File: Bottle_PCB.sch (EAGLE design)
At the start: 78 parts, among them J1 GROVE-4P-2.0-SMD, Q1 8.000 MHz, Q2 ZVN 3306 F, Q3 ZVN 3306 F, Q4 ZVN 3306 F, Q5 ZVN 3306 F, Q6 ZVN 3306 F, Q7 ZVN 3306 F, U1 USD-SOCKETNEW

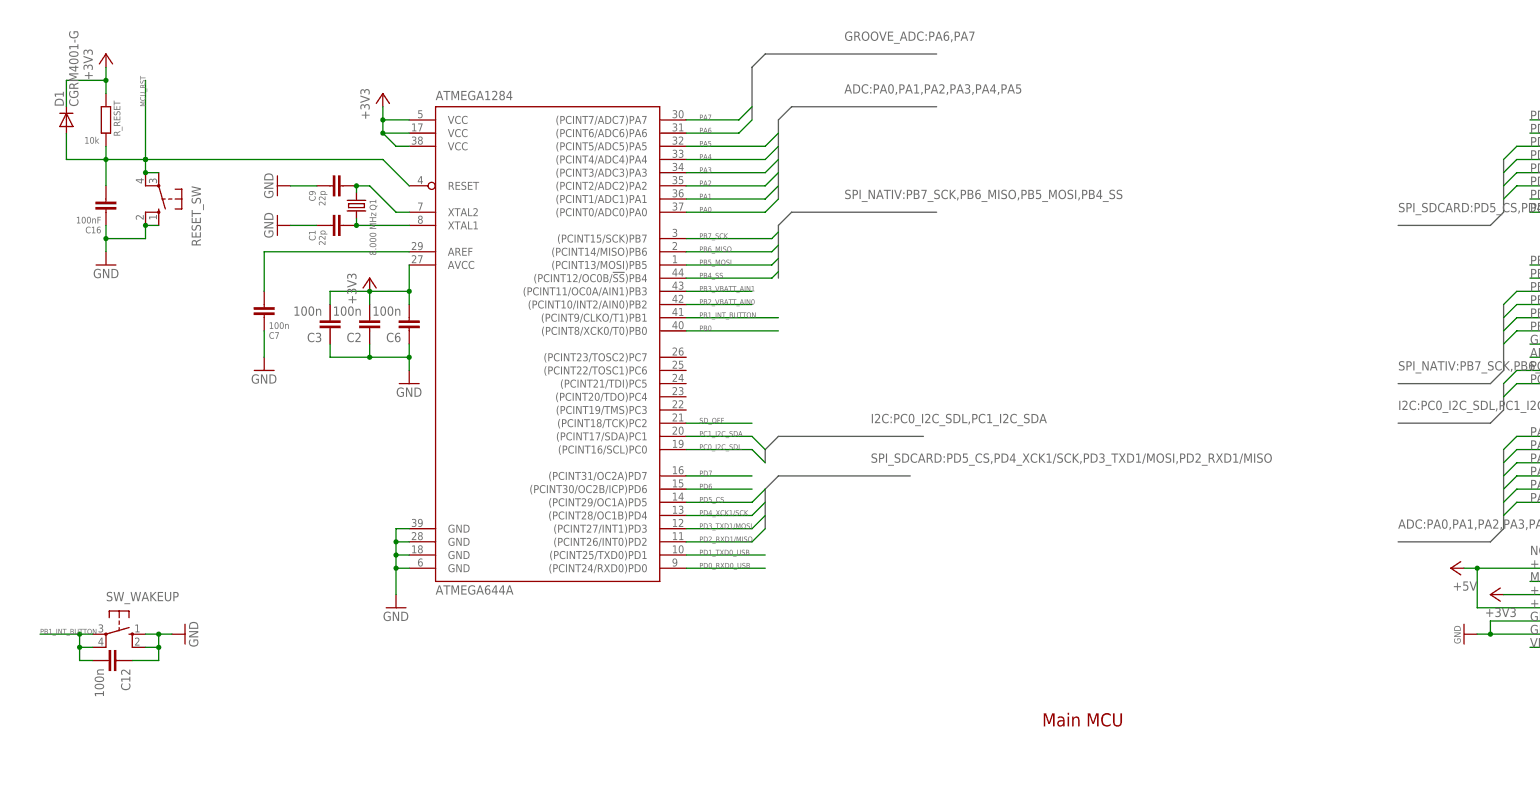
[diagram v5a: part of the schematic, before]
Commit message: - added some more frames for structure
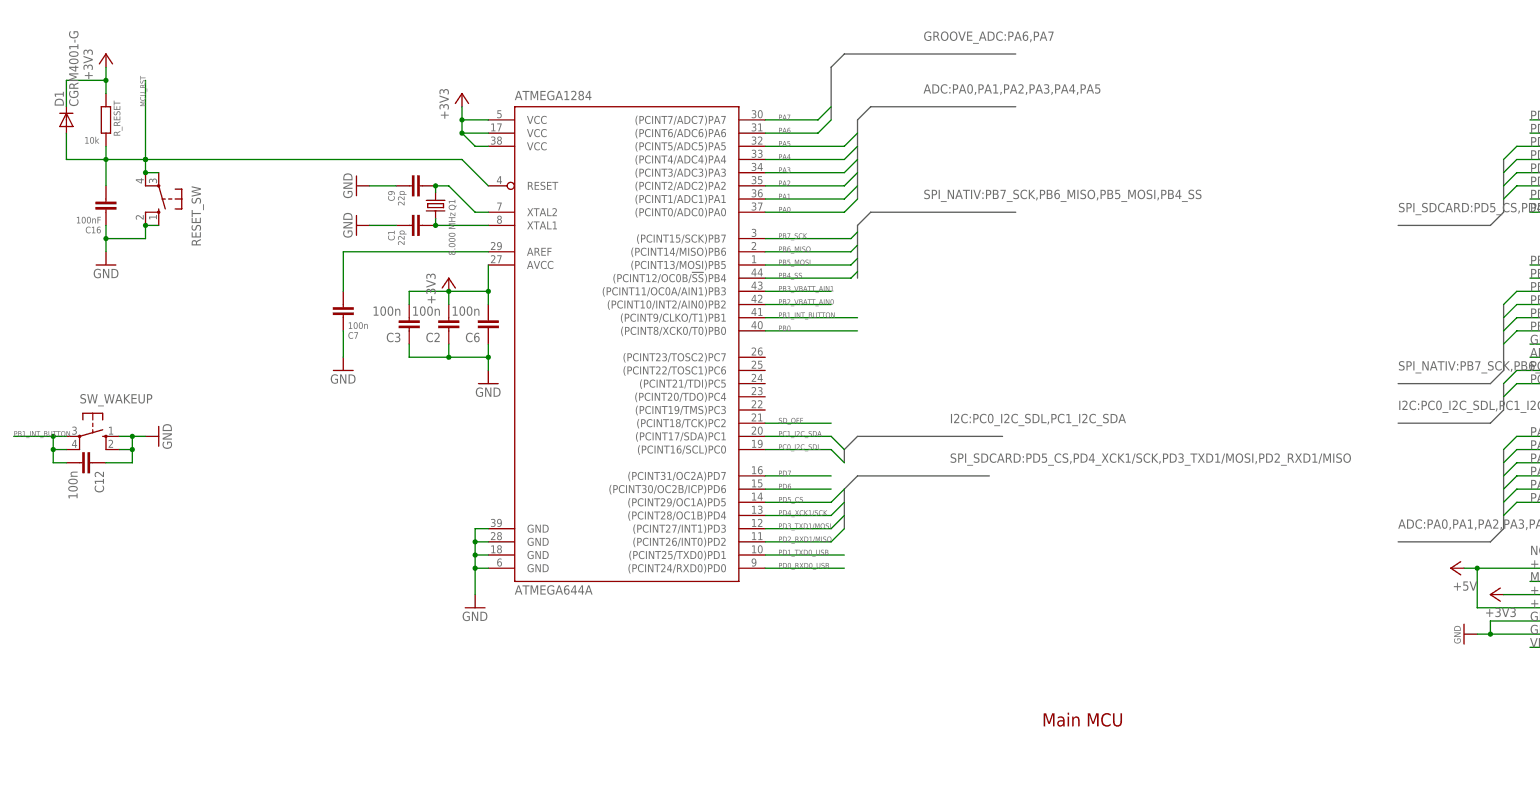
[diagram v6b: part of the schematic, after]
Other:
- note added: "MCU Reset"
- note added: "Main Microcontroller Unit"
- moved on the sheet: ATMEGA1284, C1, C12, C2, C3, C6, C7, C9, Q1, SW_WAKEUP

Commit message: - overhauled and simplified SD card connection - decided to stick with the sparkfun socket, as it's cheap and available by now
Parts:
- removed Q2, Q3, Q4: ZVN 3306 F, transistor-small-signal:BSS123
- removed R1: 50k, rcl:R-EU_M1206
- removed SJ1, SJ2: (no value), jumper:SJ2W
- R2: value 50k -> 10k
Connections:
- net SD_OFF renamed PC2_SD_OFF
- removed net N$16: SJ2.2, U1.SHIELD@2
- removed net N$17: SJ1.2, U1.SHIELD@4
- removed net N$21: R1.2, SJ2.3
- removed net N$22: R2.2, SJ1.1
- removed net N$28: Q4.D, U1.CS
- removed net N$29: Q3.D, U1.DI
- removed net N$30: Q2.D, U1.SCK
- new net PC3_SD_CD: ATMEGA1284.(PCINT19/TMS)PC3, R2.2, U1.SHIELD@2, U1.SHIELD@4
- net +3V3: no longer R1.1
- net GND: no longer SJ1.3, SJ2.1
- net N$33: no longer Q2.G, Q3.G, Q4.G
- net PD3_TXD1/MOSI: now also U1.DI; no longer Q3.S
- net PD4_XCK1/SCK: now also U1.SCK; no longer Q2.S
- net PD5_CS: now also U1.CS; no longer Q4.S
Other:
- note added: "CD pins are connected to GND when no card is insertet, and float if card is inserted. Thus, a pullup is needed for detection."
- moved on the sheet: C4, C5, Q5, R2, R5, R6, U1

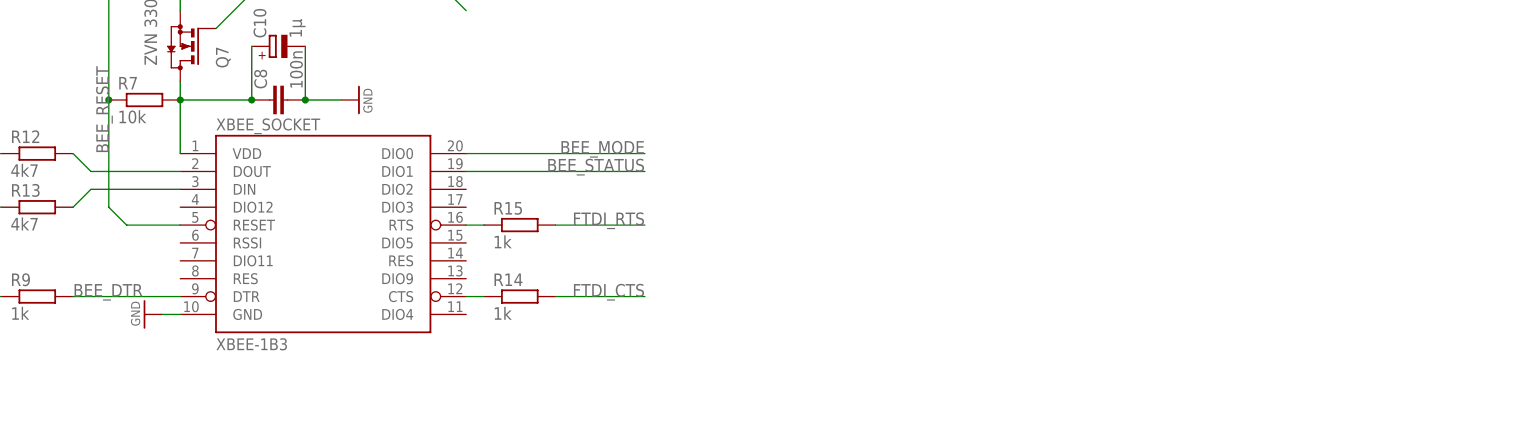
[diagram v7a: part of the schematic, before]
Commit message: - added HM11 BT Module - employed component device exported from SeedStudio BLE_Bee_v1.0 schematic
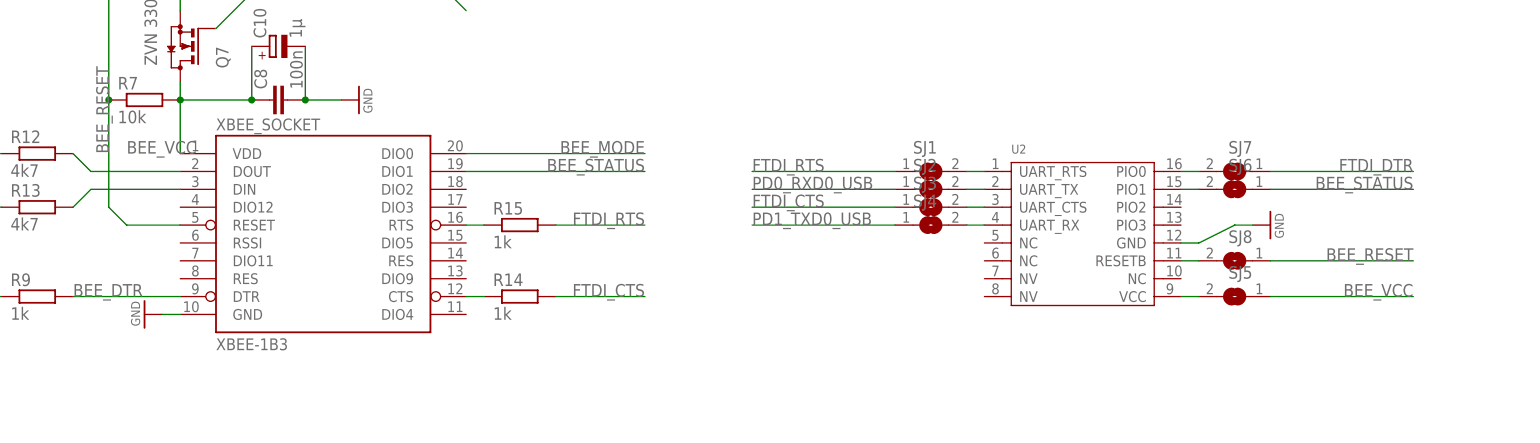
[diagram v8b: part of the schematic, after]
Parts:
- added SJ1, SJ2, SJ3, SJ4, SJ5, SJ6, SJ7, SJ8: (no value), jumper:SJ
- added U2: (no value), Seed-HM11:HM-11
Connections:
- new net N$16: SJ1.2, U2.UART_RTS
- new net N$17: SJ2.2, U2.UART_TX
- new net N$19: SJ3.2, U2.UART_CTS
- new net N$20: SJ4.2, U2.UART_RX
- new net N$21: SJ5.2, U2.VCC
- new net N$24: SJ8.2, U2.RESETB
- new net N$25: SJ6.2, U2.PIO1
- new net N$26: SJ7.2, U2.PIO0
- net BEE_RESET: now also SJ8.1
- net BEE_STATUS: now also SJ6.1
- net BEE_VCC: now also SJ5.1
- net FTDI_CTS: now also SJ3.1
- net FTDI_DTR: now also SJ7.1
- net FTDI_RTS: now also SJ1.1
- net GND: now also U2.GND
- net PD0_RXD0_USB: now also SJ2.1
- net PD1_TXD0_USB: now also SJ4.1
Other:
- note added: "HM11 BT Module"
- note removed: "BTBee Pro"
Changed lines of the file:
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@@
 <layer number="56" name="wert" color="7" fill="1" visible="no" active="no"/>
 <layer number="57" name="tCAD" color="7" fill="1" visible="no" active="no"/>
+<layer number="90" name="Modules" color="5" fill="1" visible="yes" active="yes"/>
 <layer number="91" name="Nets" color="2" fill="1" visible="yes" active="yes"/>
 <layer number="92" name="Busses" color="1" fill="1" visible="yes" active="yes"/>
@@
 <part name="R14" library="resistor" deviceset="R-EU_" device="R0603" value="1k"/>
 <part name="R15" library="resistor" deviceset="R-EU_" device="R0603" value="1k"/>
+<part name="U2" library="Seed-HM11" deviceset="HM-11" device=""/>
+<part name="SJ1" library="jumper" deviceset="SJ" device=""/>
+<part name="SJ2" library="jumper" deviceset="SJ" device=""/>
+<part name="SJ3" library="jumper" deviceset="SJ" device=""/>
+<part name="SJ4" library="jumper" deviceset="SJ" device=""/>
+<part name="SJ5" library="jumper" deviceset="SJ" device=""/>
+<part name="SJ6" library="jumper" deviceset="SJ" device=""/>
+<part name="SJ7" library="jumper" deviceset="SJ" device=""/>
+<part name="GND7" library="supply1" deviceset="GND" device=""/>
+<part name="SJ8" library="jumper" deviceset="SJ" device=""/>
 </parts>
 <sheets>
@@
 <text x="151.765" y="286.385" size="0.8128" layer="250" rot="R90">(PDO/MISO)</text>
 <wire x1="368.3" y1="345.44" x2="411.48" y2="345.44" width="0.3048" layer="104" style="shortdash"/>
-<wire x1="287.02" y1="154.94" x2="419.1" y2="154.94" width="0.3048" layer="104" style="shortdash"/>
-<wire x1="419.1" y1="154.94" x2="508" y2="154.94" width="0.3048" layer="104" style="shortdash"/>
+<wire x1="287.02" y1="154.94" x2="406.4" y2="154.94" width="0.3048" layer="104" style="shortdash"/>
+<wire x1="406.4" y1="154.94" x2="508" y2="154.94" width="0.3048" layer="104" style="shortdash"/>
 <wire x1="281.94" y1="149.86" x2="287.02" y2="154.94" width="0.3048" layer="104" style="shortdash" curve="-90"/>
 <wire x1="281.94" y1="48.26" x2="281.94" y2="149.86" width="0.3048" layer="104" style="shortdash"/>
-<wire x1="287.02" y1="43.18" x2="419.1" y2="43.18" width="0.3048" layer="104" style="shortdash"/>
-<wire x1="419.1" y1="43.18" x2="508" y2="43.18" width="0.3048" layer="104" style="shortdash"/>
+<wire x1="287.02" y1="43.18" x2="406.4" y2="43.18" width="0.3048" layer="104" style="shortdash"/>
+<wire x1="406.4" y1="43.18" x2="508" y2="43.18" width="0.3048" layer="104" style="shortdash"/>
 <wire x1="281.94" y1="47.625" x2="286.385" y2="43.18" width="0.3048" layer="104" style="shortdash" curve="90"/>
 <wire x1="288.29" y1="146.05" x2="326.39" y2="146.05" width="0.3048" layer="104"/>
 <text x="289.56" y="147.32" size="3.81" layer="104" font="vector" ratio="12">XBEE Socket</text>
 <wire x1="508" y1="154.94" x2="513.08" y2="149.86" width="0.3048" layer="104" style="shortdash" curve="-90"/>
-<wire x1="419.1" y1="43.18" x2="419.1" y2="154.94" width="0.3048" layer="104" style="shortdash"/>
+<wire x1="406.4" y1="43.18" x2="406.4" y2="154.94" width="0.3048" layer="104" style="shortdash"/>
 <wire x1="513.08" y1="48.26" x2="513.08" y2="149.86" width="0.3048" layer="104" style="shortdash"/>
-<wire x1="427.99" y1="146.05" x2="461.01" y2="146.05" width="0.3048" layer="104"/>
-<text x="429.26" y="147.32" size="3.81" layer="104" font="vector" ratio="12">BTBee Pro</text>
+<wire x1="415.29" y1="146.05" x2="463.55" y2="146.05" width="0.3048" layer="104"/>
+<text x="416.56" y="147.32" size="3.81" layer="104" font="vector" ratio="12">HM11 BT Module</text>
 <wire x1="508" y1="43.18" x2="513.08" y2="48.26" width="0.3048" layer="104" style="shortdash" curve="90"/>
 <wire x1="556.26" y1="350.52" x2="635" y2="350.52" width="0.3048" layer="104" style="shortdash"/>
@@
 <instance part="R14" gate="G$1" x="381" y="68.58"/>
 <instance part="R15" gate="G$1" x="381" y="78.74"/>
+<instance part="U2" gate="G$1" x="461.01" y="77.47"/>
+<instance part="SJ1" gate="1" x="439.42" y="86.36"/>
+<instance part="SJ2" gate="1" x="439.42" y="83.82"/>
+<instance part="SJ3" gate="1" x="439.42" y="81.28"/>
+<instance part="SJ4" gate="1" x="439.42" y="78.74"/>
+<instance part="SJ5" gate="1" x="482.6" y="68.58" rot="MR0"/>
+<instance part="SJ6" gate="1" x="482.6" y="83.82" rot="MR0"/>
+<instance part="SJ7" gate="1" x="482.6" y="86.36" rot="MR0"/>
+<instance part="GND7" gate="1" x="487.68" y="78.74" smashed="yes" rot="R90">
+<attribute name="VALUE" x="489.585" y="76.835" size="1.27" layer="96" rot="R90"/>
+</instance>
+<instance part="SJ8" gate="1" x="482.6" y="73.66" rot="MR0"/>
 </instances>
 <busses>
@@
 <pinref part="GND16" gate="1" pin="GND"/>
 </segment>
+<segment>
+<pinref part="U2" gate="G$1" pin="GND"/>
+<pinref part="GND7" gate="1" pin="GND"/>
+<wire x1="485.14" y1="78.74" x2="482.6" y2="78.74" width="0.1524" layer="91"/>
+<wire x1="482.6" y1="78.74" x2="477.52" y2="76.2" width="0.1524" layer="91"/>
+<wire x1="477.52" y1="76.2" x2="474.98" y2="76.2" width="0.1524" layer="91"/>
+</segment>
 </net>
 <net name="AREF" class="0">
@@
 <wire x1="307.34" y1="68.58" x2="287.02" y2="68.58" width="0.1524" layer="91"/>
 <label x="287.02" y="68.58" size="1.778" layer="95"/>
+</segment>
+<segment>
+<wire x1="487.68" y1="86.36" x2="508" y2="86.36" width="0.1524" layer="91"/>
+<pinref part="SJ7" gate="1" pin="1"/>
+<label x="508" y="86.36" size="1.778" layer="95" rot="MR0"/>
 </segment>
 </net>
@@
 <label x="378.46" y="228.6" size="1.016" layer="95"/>
 </segment>
+<segment>
+<wire x1="434.34" y1="78.74" x2="414.02" y2="78.74" width="0.1524" layer="91"/>
+<label x="414.02" y="78.74" size="1.778" layer="95"/>
+<pinref part="SJ4" gate="1" pin="1"/>
+</segment>
 </net>
 <net name="PB4_SS" class="0">
@@
 <label x="378.46" y="226.06" size="1.016" layer="95"/>
 </segment>
+<segment>
+<wire x1="434.34" y1="83.82" x2="414.02" y2="83.82" width="0.1524" layer="91"/>
+<label x="414.02" y="83.82" size="1.778" layer="95"/>
+<pinref part="SJ2" gate="1" pin="1"/>
+</segment>
 </net>
 <net name="PD6" class="0">
@@
 <junction x="322.58" y="96.52"/>
 </segment>
+<segment>
+<wire x1="487.68" y1="73.66" x2="508" y2="73.66" width="0.1524" layer="91"/>
+<pinref part="SJ8" gate="1" pin="1"/>
+<label x="508" y="73.66" size="1.778" layer="95" rot="MR0"/>
+</segment>
 </net>
 <net name="BEE_VCC" class="0">
@@
 <junction x="342.9" y="96.52"/>
 <wire x1="332.74" y1="96.52" x2="342.9" y2="96.52" width="0.1524" layer="91"/>
+<label x="325.12" y="88.9" size="1.778" layer="95"/>
+</segment>
+<segment>
+<wire x1="508" y1="68.58" x2="487.68" y2="68.58" width="0.1524" layer="91"/>
+<label x="508" y="68.58" size="1.778" layer="95" rot="MR0"/>
+<pinref part="SJ5" gate="1" pin="1"/>
 </segment>
 </net>
@@
 <label x="398.78" y="86.36" size="1.778" layer="95" rot="MR0"/>
 </segment>
+<segment>
+<wire x1="487.68" y1="83.82" x2="508" y2="83.82" width="0.1524" layer="91"/>
+<pinref part="SJ6" gate="1" pin="1"/>
+<label x="508" y="83.82" size="1.778" layer="95" rot="MR0"/>
+</segment>
 </net>
 <net name="BEE_MODE" class="0">
@@
 <label x="398.78" y="68.58" size="1.778" layer="95" rot="MR0"/>
 </segment>
+<segment>
+<wire x1="434.34" y1="81.28" x2="414.02" y2="81.28" width="0.1524" layer="91"/>
+<label x="414.02" y="81.28" size="1.778" layer="95"/>
+<pinref part="SJ3" gate="1" pin="1"/>
+</segment>
 </net>
 <net name="N$5" class="0">
@@
 <label x="398.78" y="78.74" size="1.778" layer="95" rot="MR0"/>
 </segment>
+<segment>
+<wire x1="434.34" y1="86.36" x2="414.02" y2="86.36" width="0.1524" layer="91"/>
+<label x="414.02" y="86.36" size="1.778" layer="95"/>
+<pinref part="SJ1" gate="1" pin="1"/>
+</segment>
 </net>
 <net name="N$7" class="0">
@@
 </segment>
 </net>
+<net name="N$16" class="0">
+<segment>
+<pinref part="SJ1" gate="1" pin="2"/>
+<pinref part="U2" gate="G$1" pin="UART_RTS"/>
+<wire x1="447.04" y1="86.36" x2="444.5" y2="86.36" width="0.1524" layer="91"/>
+</segment>
+</net>
+<net name="N$17" class="0">
+<segment>
+<pinref part="SJ2" gate="1" pin="2"/>
+<pinref part="U2" gate="G$1" pin="UART_TX"/>
+<wire x1="447.04" y1="83.82" x2="444.5" y2="83.82" width="0.1524" layer="91"/>
+</segment>
+</net>
+<net name="N$19" class="0">
+<segment>
+<pinref part="SJ3" gate="1" pin="2"/>
+<pinref part="U2" gate="G$1" pin="UART_CTS"/>
+<wire x1="447.04" y1="81.28" x2="444.5" y2="81.28" width="0.1524" layer="91"/>
+</segment>
+</net>
+<net name="N$20" class="0">
+<segment>
+<pinref part="SJ4" gate="1" pin="2"/>
+<pinref part="U2" gate="G$1" pin="UART_RX"/>
+<wire x1="447.04" y1="78.74" x2="444.5" y2="78.74" width="0.1524" layer="91"/>
+</segment>
+</net>
+<net name="N$21" class="0">
+<segment>
+<pinref part="U2" gate="G$1" pin="VCC"/>
+<pinref part="SJ5" gate="1" pin="2"/>
+<wire x1="474.98" y1="68.58" x2="477.52" y2="68.58" width="0.1524" layer="91"/>
+</segment>
+</net>
+<net name="N$24" class="0">
+<segment>
+<pinref part="SJ8" gate="1" pin="2"/>
+<pinref part="U2" gate="G$1" pin="RESETB"/>
+<wire x1="477.52" y1="73.66" x2="474.98" y2="73.66" width="0.1524" layer="91"/>
+</segment>
+</net>
+<net name="N$25" class="0">
+<segment>
+<pinref part="U2" gate="G$1" pin="PIO1"/>
+<pinref part="SJ6" gate="1" pin="2"/>
+<wire x1="477.52" y1="83.82" x2="474.98" y2="83.82" width="0.1524" layer="91"/>
+</segment>
+</net>
+<net name="N$26" class="0">
+<segment>
+<pinref part="U2" gate="G$1" pin="PIO0"/>
+<pinref part="SJ7" gate="1" pin="2"/>
+<wire x1="477.52" y1="86.36" x2="474.98" y2="86.36" width="0.1524" layer="91"/>
+</segment>
+</net>
